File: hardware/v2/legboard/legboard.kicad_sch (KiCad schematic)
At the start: 17 parts, among them J1 UPLINK_RJ11, J2 COXA, J3 FEMUR, J4 TIBIA, J5 SERVO_PWR_IN, U1 XIAO-RP2040, U2 SP3485CN, U3 INA4181A3IPWR

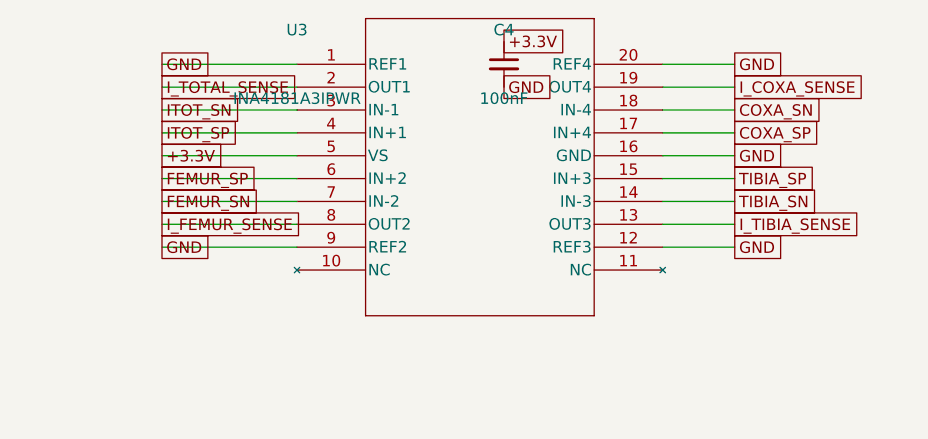
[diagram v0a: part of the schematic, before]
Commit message: hardware: fix legboard current-sense channel mapping, swap powerboard PMOS to IRF9540NPBF
Legboard: correct the INA4181 stub labels so U3 pins 2-4/13-15 map to
TOTAL/TIBIA current sensing per the corrected net table, instead of the
swapped TOTAL<->TIBIA assignment.

Powerboard: replace Q1/Q2 reverse-polarity PMOS (FQP47P06 -> IRF9540NPBF).
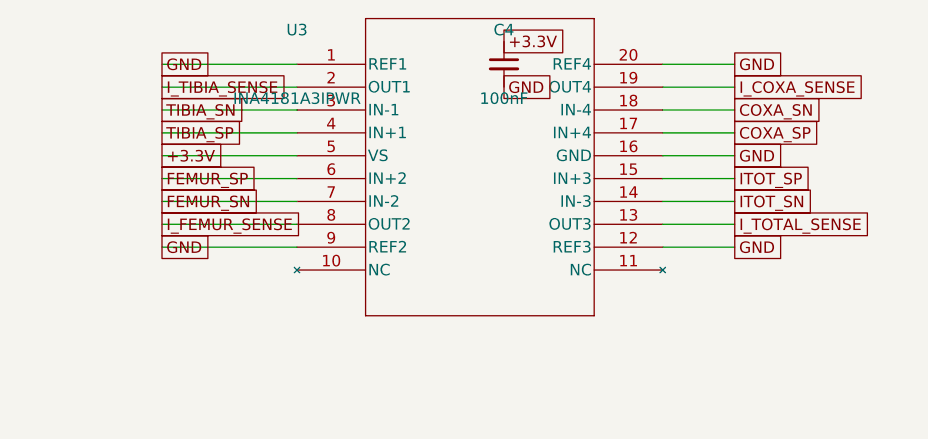
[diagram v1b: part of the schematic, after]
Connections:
- net ITOT_SN: now also U3.14 (IN-3); no longer U3.3 (IN-1)
- net ITOT_SP: now also U3.15 (IN+3); no longer U3.4 (IN+1)
- net I_TIBIA_SENSE: now also U3.2 (OUT1); no longer U3.13 (OUT3)
- net I_TOTAL_SENSE: now also U3.13 (OUT3); no longer U3.2 (OUT1)
- net TIBIA_SN: now also U3.3 (IN-1); no longer U3.14 (IN-3)
- net TIBIA_SP: now also U3.4 (IN+1); no longer U3.15 (IN+3)
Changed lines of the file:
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@@
+		)
+	)
+	(global_label "I_TIBIA_SENSE"
+		(shape passive)
+		(at 210 42.54 0)
+		(fields_autoplaced yes)
+		(effects
+			(font
+				(size 1.27 1.27)
+			)
+			(justify left)
+		)
+	)
+	(wire
+		(pts
+			(xy 225 45.08) (xy 210 45.08)
+		)
+		(stroke
+			(width 0)
+			(type default)
+		)
+	)
+	(global_label "TIBIA_SN"
+		(shape passive)
+		(at 210 45.08 0)
+		(fields_autoplaced yes)
+		(effects
+			(font
+				(size 1.27 1.27)
+			)
+			(justify left)
+		)
+	)
+	(wire
+		(pts
+			(xy 225 47.62) (xy 210 47.62)
+		)
+		(stroke
+			(width 0)
+			(type default)
+		)
+	)
+	(global_label "TIBIA_SP"
+		(shape passive)
+		(at 210 47.62 0)
+		(fields_autoplaced yes)
+		(effects
+			(font
+				(size 1.27 1.27)
+			)
+			(justify left)
+		)
+	)
+	(wire
+		(pts
+			(xy 225 50.16) (xy 210 50.16)
+		)
+		(stroke
+			(width 0)
+			(type default)
+		)
+	)
+	(global_label "+3.3V"
+		(shape passive)
+		(at 210 50.16 0)
+		(fields_autoplaced yes)
+		(effects
+			(font
+				(size 1.27 1.27)
+			)
+			(justify left)
+		)
+	)
+	(wire
+		(pts
+			(xy 225 52.7) (xy 210 52.7)
+		)
+		(stroke
+			(width 0)
+			(type default)
+		)
+	)
+	(global_label "FEMUR_SP"
+		(shape passive)
+		(at 210 52.7 0)
+		(fields_autoplaced yes)
+		(effects
+			(font
+				(size 1.27 1.27)
+			)
+			(justify left)
+		)
+	)
+	(wire
+		(pts
+			(xy 225 55.24) (xy 210 55.24)
+		)
+		(stroke
+			(width 0)
+			(type default)
+		)
+	)
+	(global_label "FEMUR_SN"
+		(shape passive)
+		(at 210 55.24 0)
+		(fields_autoplaced yes)
+		(effects
+			(font
+				(size 1.27 1.27)
+			)
+			(justify left)
+		)
+	)
+	(wire
+		(pts
+			(xy 225 57.78) (xy 210 57.78)
+		)
+		(stroke
+			(width 0)
+			(type default)
+		)
+	)
+	(global_label "I_FEMUR_SENSE"
+		(shape passive)
+		(at 210 57.78 0)
+		(fields_autoplaced yes)
+		(effects
+			(font
+				(size 1.27 1.27)
+			)
+			(justify left)
+		)
+	)
+	(wire
+		(pts
+			(xy 225 60.32) (xy 210 60.32)
+		)
+		(stroke
+			(width 0)
+			(type default)
+		)
+	)
+	(global_label "GND"
+		(shape passive)
+		(at 210 60.32 0)
+		(fields_autoplaced yes)
+		(effects
+			(font
+				(size 1.27 1.27)
+			)
+			(justify left)
+		)
+	)
+	(wire
+		(pts
+			(xy 265.64 60.32) (xy 273.64 60.32)
+		)
+		(stroke
+			(width 0)
+			(type default)
+		)
+	)
+	(global_label "GND"
+		(shape passive)
+		(at 273.64 60.32 0)
+		(fields_autoplaced yes)
+		(effects
+			(font
+				(size 1.27 1.27)
+			)
+			(justify left)
+		)
+	)
+	(wire
+		(pts
+			(xy 265.64 57.78) (xy 273.64 57.78)
+		)
+		(stroke
+			(width 0)
+			(type default)
 		)
 	)
 	(global_label "I_TOTAL_SENSE"
 		(shape passive)
-		(at 210 42.54 0)
-		(fields_autoplaced yes)
-		(effects
-			(font
-				(size 1.27 1.27)
-			)
-			(justify left)
-		)
-	)
-	(wire
-		(pts
-			(xy 225 45.08) (xy 210 45.08)
+		(at 273.64 57.78 0)
+		(fields_autoplaced yes)
+		(effects
+			(font
+				(size 1.27 1.27)
+			)
+			(justify left)
+		)
+	)
+	(wire
+		(pts
+			(xy 265.64 55.24) (xy 273.64 55.24)
 		)
 		(stroke
@@
 	(global_label "ITOT_SN"
 		(shape passive)
-		(at 210 45.08 0)
-		(fields_autoplaced yes)
-		(effects
-			(font
-				(size 1.27 1.27)
-			)
-			(justify left)
-		)
-	)
-	(wire
-		(pts
-			(xy 225 47.62) (xy 210 47.62)
+		(at 273.64 55.24 0)
+		(fields_autoplaced yes)
+		(effects
+			(font
+				(size 1.27 1.27)
+			)
+			(justify left)
+		)
+	)
+	(wire
+		(pts
+			(xy 265.64 52.7) (xy 273.64 52.7)
 		)
 		(stroke
@@
 	(global_label "ITOT_SP"
 		(shape passive)
-		(at 210 47.62 0)
-		(fields_autoplaced yes)
-		(effects
-			(font
-				(size 1.27 1.27)
-			)
-			(justify left)
-		)
-	)
-	(wire
-		(pts
-			(xy 225 50.16) (xy 210 50.16)
-		)
-		(stroke
-			(width 0)
-			(type default)
-		)
-	)
-	(global_label "+3.3V"
-		(shape passive)
-		(at 210 50.16 0)
-		(fields_autoplaced yes)
-		(effects
-			(font
-				(size 1.27 1.27)
-			)
-			(justify left)
-		)
-	)
-	(wire
-		(pts
-			(xy 225 52.7) (xy 210 52.7)
-		)
-		(stroke
-			(width 0)
-			(type default)
-		)
-	)
-	(global_label "FEMUR_SP"
-		(shape passive)
-		(at 210 52.7 0)
-		(fields_autoplaced yes)
-		(effects
-			(font
-				(size 1.27 1.27)
-			)
-			(justify left)
-		)
-	)
-	(wire
-		(pts
-			(xy 225 55.24) (xy 210 55.24)
-		)
-		(stroke
-			(width 0)
-			(type default)
-		)
-	)
-	(global_label "FEMUR_SN"
-		(shape passive)
-		(at 210 55.24 0)
-		(fields_autoplaced yes)
-		(effects
-			(font
-				(size 1.27 1.27)
-			)
-			(justify left)
-		)
-	)
-	(wire
-		(pts
-			(xy 225 57.78) (xy 210 57.78)
-		)
-		(stroke
-			(width 0)
-			(type default)
-		)
-	)
-	(global_label "I_FEMUR_SENSE"
-		(shape passive)
-		(at 210 57.78 0)
-		(fields_autoplaced yes)
-		(effects
-			(font
-				(size 1.27 1.27)
-			)
-			(justify left)
-		)
-	)
-	(wire
-		(pts
-			(xy 225 60.32) (xy 210 60.32)
-		)
-		(stroke
-			(width 0)
-			(type default)
-		)
-	)
-	(global_label "GND"
-		(shape passive)
-		(at 210 60.32 0)
-		(fields_autoplaced yes)
-		(effects
-			(font
-				(size 1.27 1.27)
-			)
-			(justify left)
-		)
-	)
-	(wire
-		(pts
-			(xy 265.64 60.32) (xy 273.64 60.32)
-		)
-		(stroke
-			(width 0)
-			(type default)
-		)
-	)
-	(global_label "GND"
-		(shape passive)
-		(at 273.64 60.32 0)
-		(fields_autoplaced yes)
-		(effects
-			(font
-				(size 1.27 1.27)
-			)
-			(justify left)
-		)
-	)
-	(wire
-		(pts
-			(xy 265.64 57.78) (xy 273.64 57.78)
-		)
-		(stroke
-			(width 0)
-			(type default)
-		)
-	)
-	(global_label "I_TIBIA_SENSE"
-		(shape passive)
-		(at 273.64 57.78 0)
-		(fields_autoplaced yes)
-		(effects
-			(font
-				(size 1.27 1.27)
-			)
-			(justify left)
-		)
-	)
-	(wire
-		(pts
-			(xy 265.64 55.24) (xy 273.64 55.24)
-		)
-		(stroke
-			(width 0)
-			(type default)
-		)
-	)
-	(global_label "TIBIA_SN"
-		(shape passive)
-		(at 273.64 55.24 0)
-		(fields_autoplaced yes)
-		(effects
-			(font
-				(size 1.27 1.27)
-			)
-			(justify left)
-		)
-	)
-	(wire
-		(pts
-			(xy 265.64 52.7) (xy 273.64 52.7)
-		)
-		(stroke
-			(width 0)
-			(type default)
-		)
-	)
-	(global_label "TIBIA_SP"
-		(shape passive)
 		(at 273.64 52.7 0)
